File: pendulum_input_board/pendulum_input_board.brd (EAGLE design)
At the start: 75 x 40 mm, 26 parts, among them IC1 FT232H, J1 PJ-051BH, U1 LTC2851MPDDPBF, X1 MINI-USB-UX60-MB-5S8, X2 SM07B-SRSS-TB, X3 SM07B-SRSS-TB

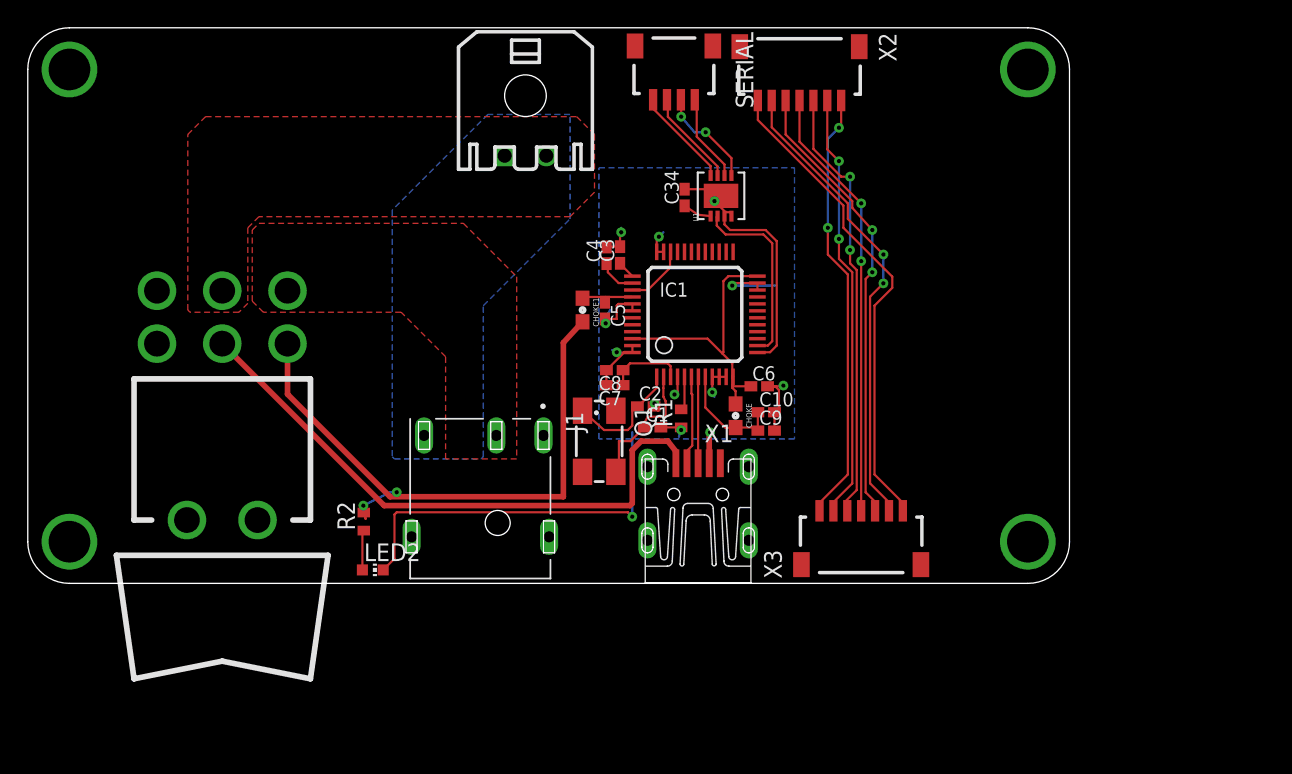
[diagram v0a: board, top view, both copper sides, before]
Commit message: Pendulum control demo in python
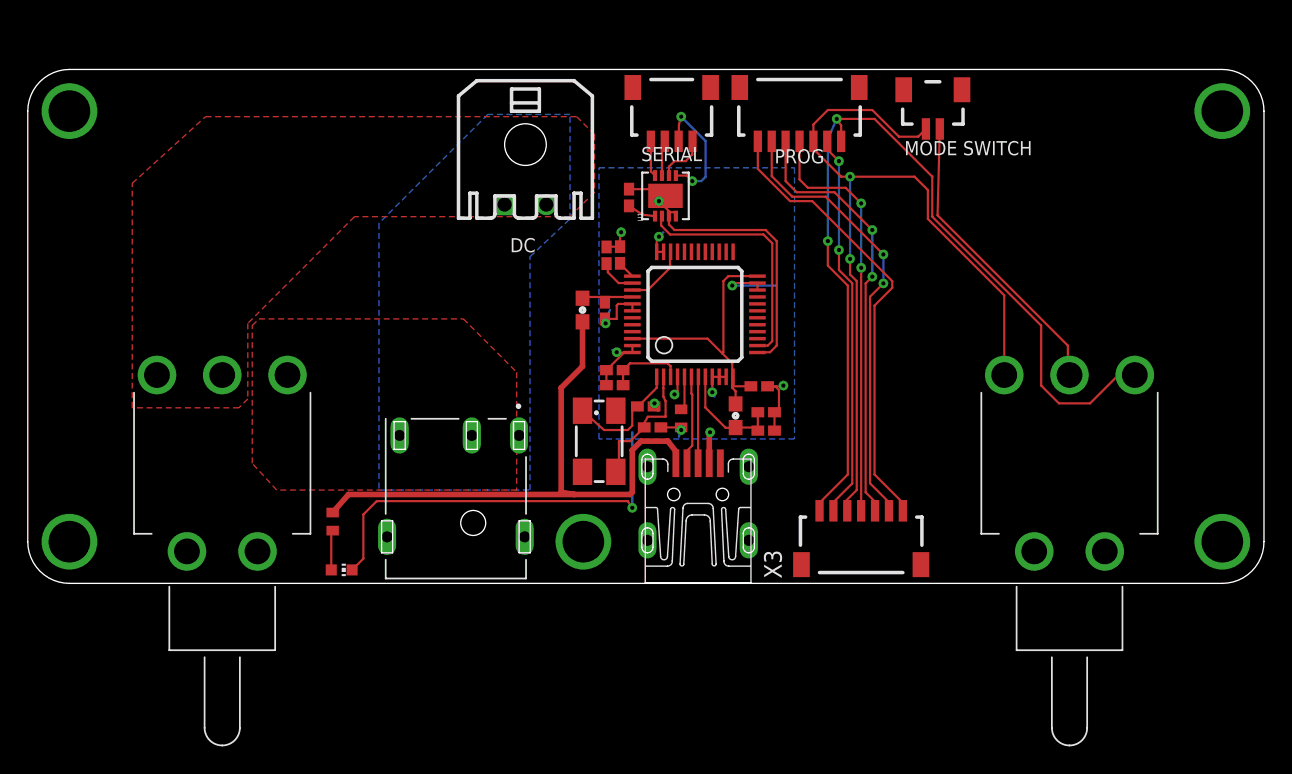
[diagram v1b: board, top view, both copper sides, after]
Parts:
- removed U$1: 7201_SWITCH, Ben_Library:7201_SWITCH
- added U$2, U$3: SPDT, Ben_Library:100SP
- added X4: SM02B-SSR-H-TB, con-jst2:SM02B-SSR-H-TB
- moved C34 4.00 mm to (43.3, 27.8)
- moved U1 4.00 mm to (45.9, 27.9)
- moved DC 3.52 mm to (35.8, 31.6)
- moved SERIAL 2.99 mm to (46.4, 34.8)
- moved X2 2.94 mm to (55.6, 34.8)
- moved R2 2.24 mm to (21.9, 4.45)
- moved LED2 2.24 mm to (22.6, 0.97)
- moved J1 1.76 mm to (30.8, 6.10)
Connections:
- removed net N$12: CHOKE1.2, R2.2, U$1.R2
- new net MODE_SWITCH: U$3.P$2, X4.1
- net +24V: now also U$2.P$2; no longer U$1.C1
- net 24V_IN: now also U$2.P$3; no longer U$1.R1
- net 3V3: now also U$3.P$3
- net 5V_IN: now also CHOKE1.2, R2.2; no longer U$1.C2
- net GND: now also U$3.P$1, X4.2
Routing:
- net N$12: track 44.4 -> 0.00 mm, vias 2 -> 0
- net 3V3: track 36.0 -> 71.1 mm
- net GND: track 101.6 -> 133.1 mm
- net MODE_SWITCH: track 0.00 -> 21.7 mm
- net SER_Y: track 7.17 -> 2.59 mm
- net SER_Z: track 6.96 -> 2.55 mm
- net SER_RX: track 13.5 -> 17.5 mm
- net SER_TX: track 14.0 -> 18.0 mm
- net TCK: track 30.9 -> 28.0 mm
- net SER_A: track 6.34 -> 3.64 mm
- net USART_RX: track 34.9 -> 32.9 mm
- net SER_B: track 7.38 -> 9.28 mm
- net USART_TX: track 33.9 -> 32.4 mm
- net TMS: track 31.4 -> 30.1 mm
- net 5V_IN: track 42.9 -> 43.8 mm
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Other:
- board size 75 x 40 mm -> 89 x 37 mm
- board text added: "DC"
- board text added: "MODE SWITCH"
- board text added: "PROG"
- board text added: "SERIAL"

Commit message: updated pendulum software
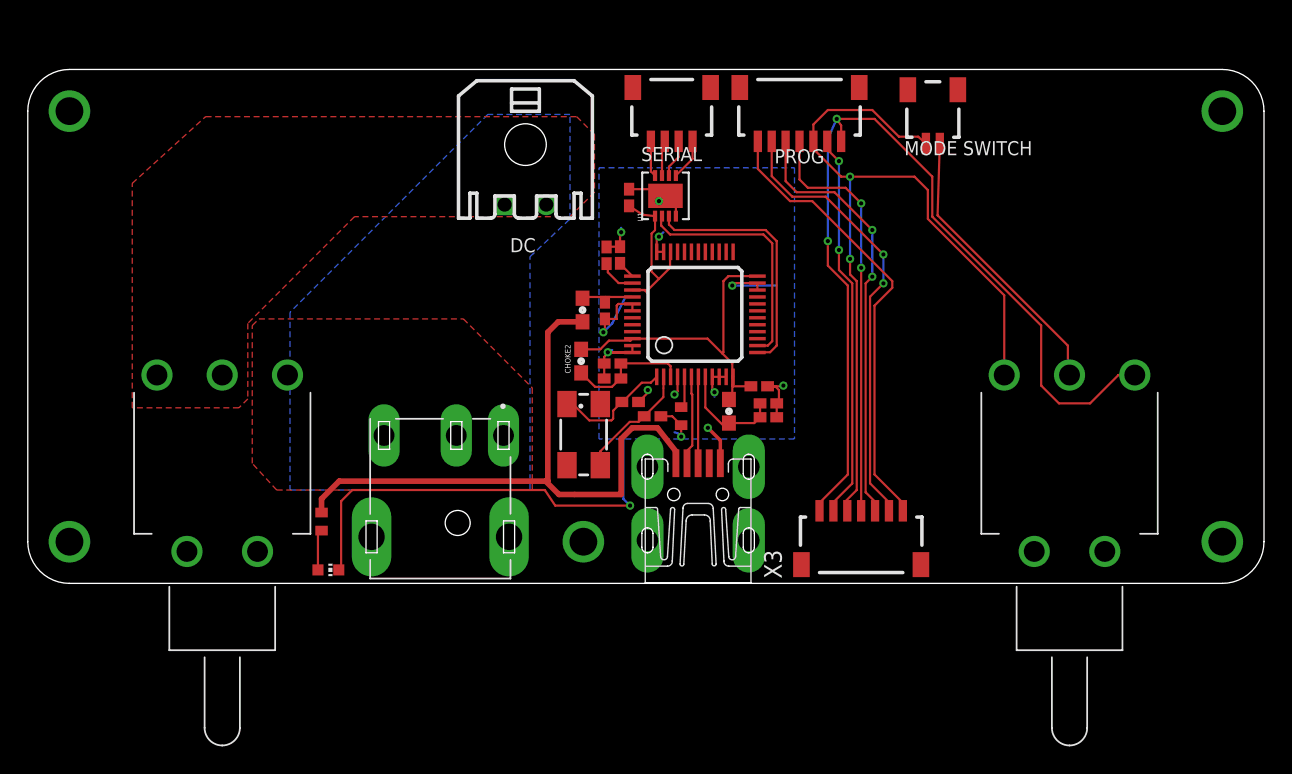
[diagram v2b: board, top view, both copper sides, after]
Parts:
- added CHOKE2: 600r, SparkFun-Passives:0603
- X4: value SM02B-SSR-H-TB -> SM02B-SRSS-TB; device con-jst2:SM02B-SSR-H-TB -> con-jst2:SM02B-SRSS-TB
- moved Q1 1.22 mm to (40.0, 10.7)
- moved C2 1.16 mm to (43.4, 13.1)
- moved J1 1.12 mm to (29.7, 6.10)
- moved C9 0.97 mm to (53.3, 12.0)
- moved LED2 0.96 mm to (21.6, 0.97)
- moved R2 0.80 mm to (21.1, 4.45)
- moved C1 0.80 mm to (45.0, 12.0)
- moved C10 0.66 mm to (53.3, 13.0)
- moved CHOKE 0.58 mm to (50.5, 12.4)
- moved C7 0.51 mm to (42.1, 14.8)
- moved C8 0.51 mm to (42.1, 15.8)
- moved R1 0.16 mm to (47.0, 12.0)
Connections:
- removed net 3V1: C34.1, U1.1
- removed net N$7: C6.1, CHOKE.1, IC1.12, IC1.24, IC1.46
- net 24V_IN: now also J1.1; no longer J1.3
- net 3V3: now also C34.1, C6.1, CHOKE.1, CHOKE2.2, IC1.12, IC1.24, IC1.46, U1.1
- net GND: now also X1.5; no longer X1.4
- net N$8: now also CHOKE2.1
- net P_GND: now also J1.3
- net SER_A: now also U1.5; no longer U1.6
- net SER_B: now also U1.6; no longer U1.5
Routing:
- net 3V3: track 71.1 -> 106.3 mm
- net N$7: track 20.2 -> 0.00 mm
- net GND: track 133.1 -> 139.7 mm
- net SER_B: track 9.28 -> 2.75 mm, vias 2 -> 0
- net N$8: track 5.56 -> 9.04 mm
- net 5V_IN: track 43.8 -> 47.1 mm
- net 3V1: track 2.07 -> 0.00 mm
- net MODE_SWITCH: track 21.7 -> 20.6 mm
- net SER_A: track 3.64 -> 2.99 mm

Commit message: fixing controller BOM mistake
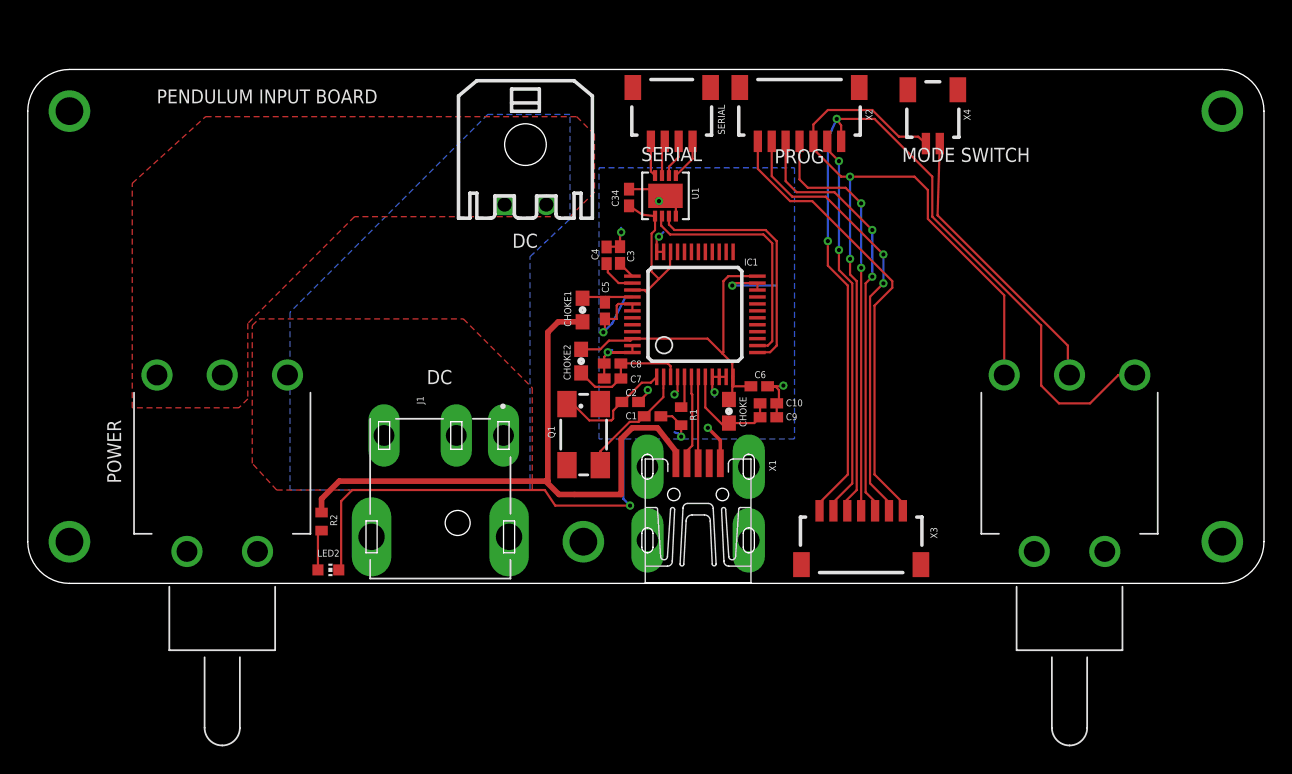
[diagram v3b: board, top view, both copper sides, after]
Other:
- board text added: "PENDULUM INPUT BOARD"
- board text added: "POWER"
